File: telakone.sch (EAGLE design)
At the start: 166 parts, among them X10 MPT0.5/8-2.54, X11 MPT0.5/8-2.54, X2 MPT0.5/8-2.54, X3 MPT0.5/8-2.54, X4 PIIKKIRIMA-2, X5 PIIKKIRIMA-5, X7 U.FL-R-SMT-1, X8 MPT0.5/8-2.54, X9 629105136821

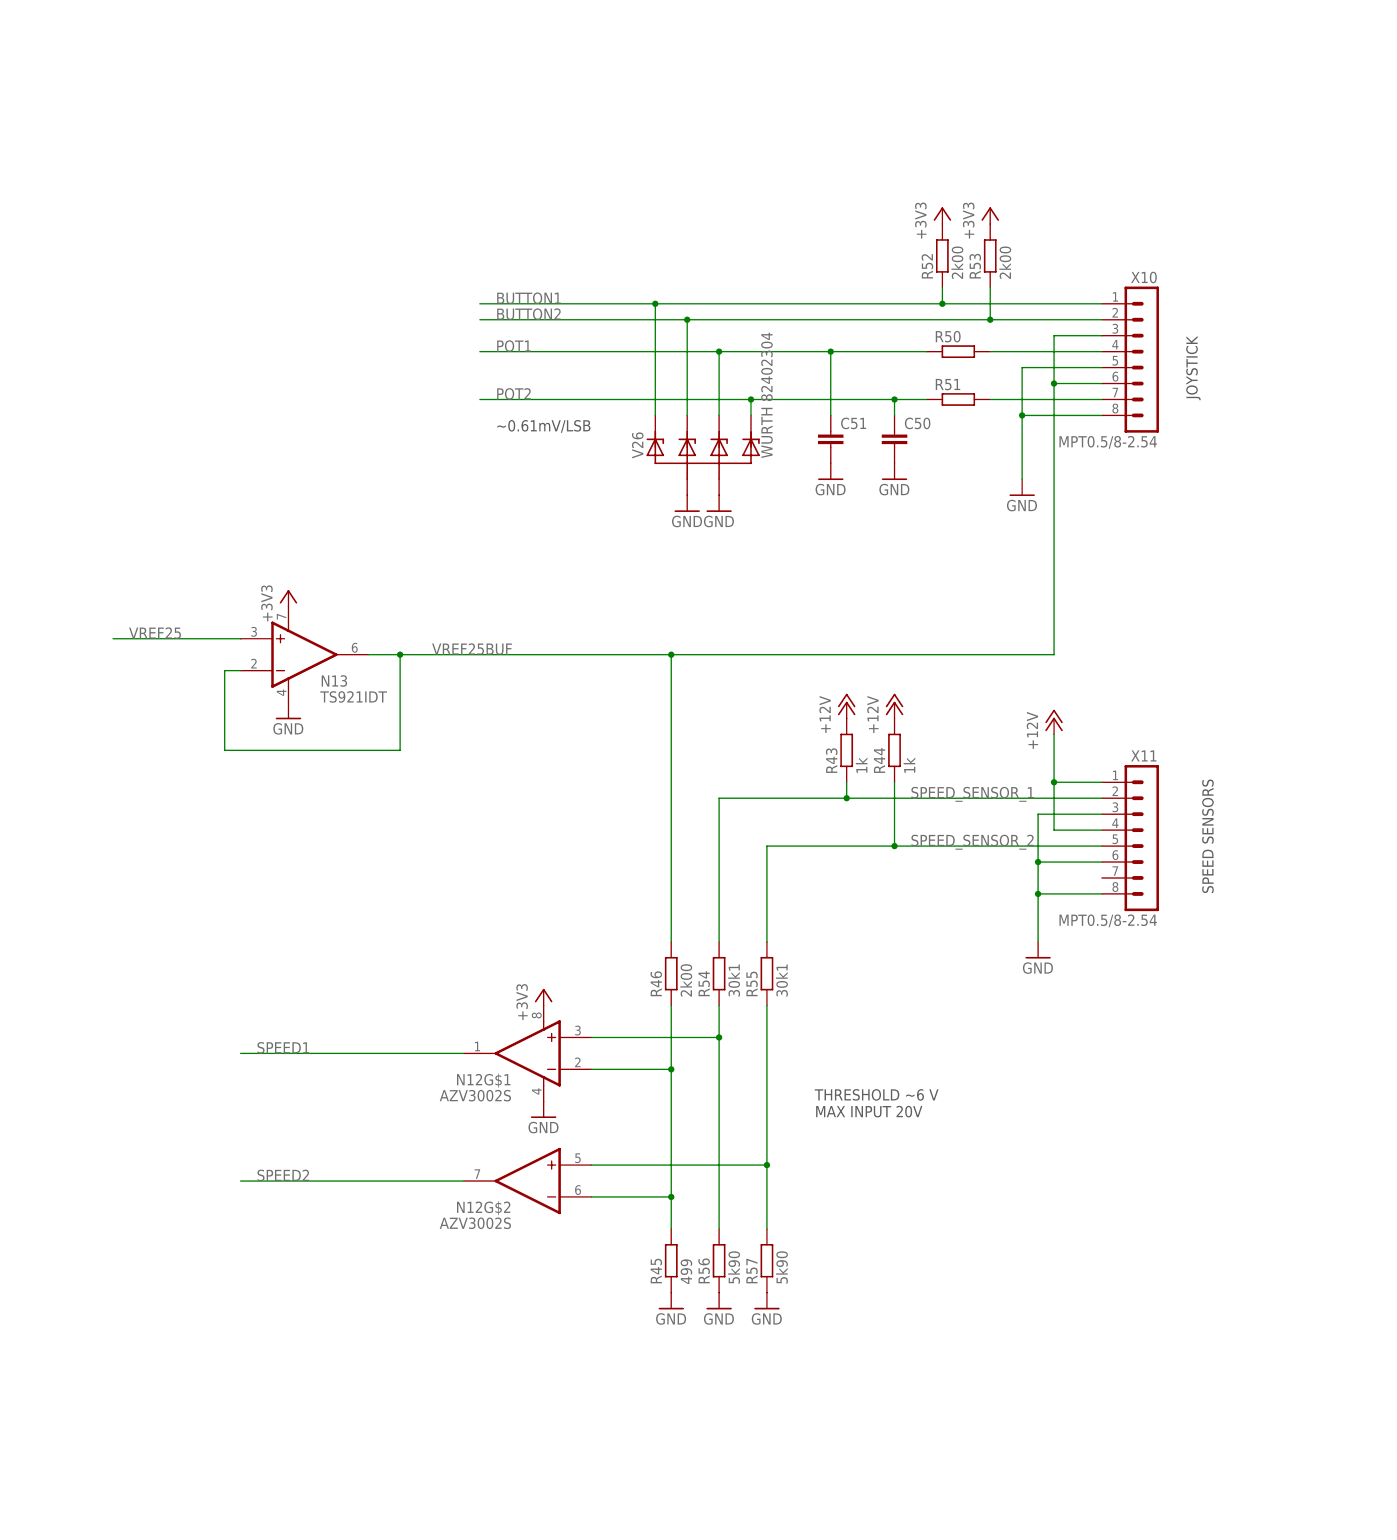
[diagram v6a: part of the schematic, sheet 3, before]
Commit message: add accessory link 485 transceiver
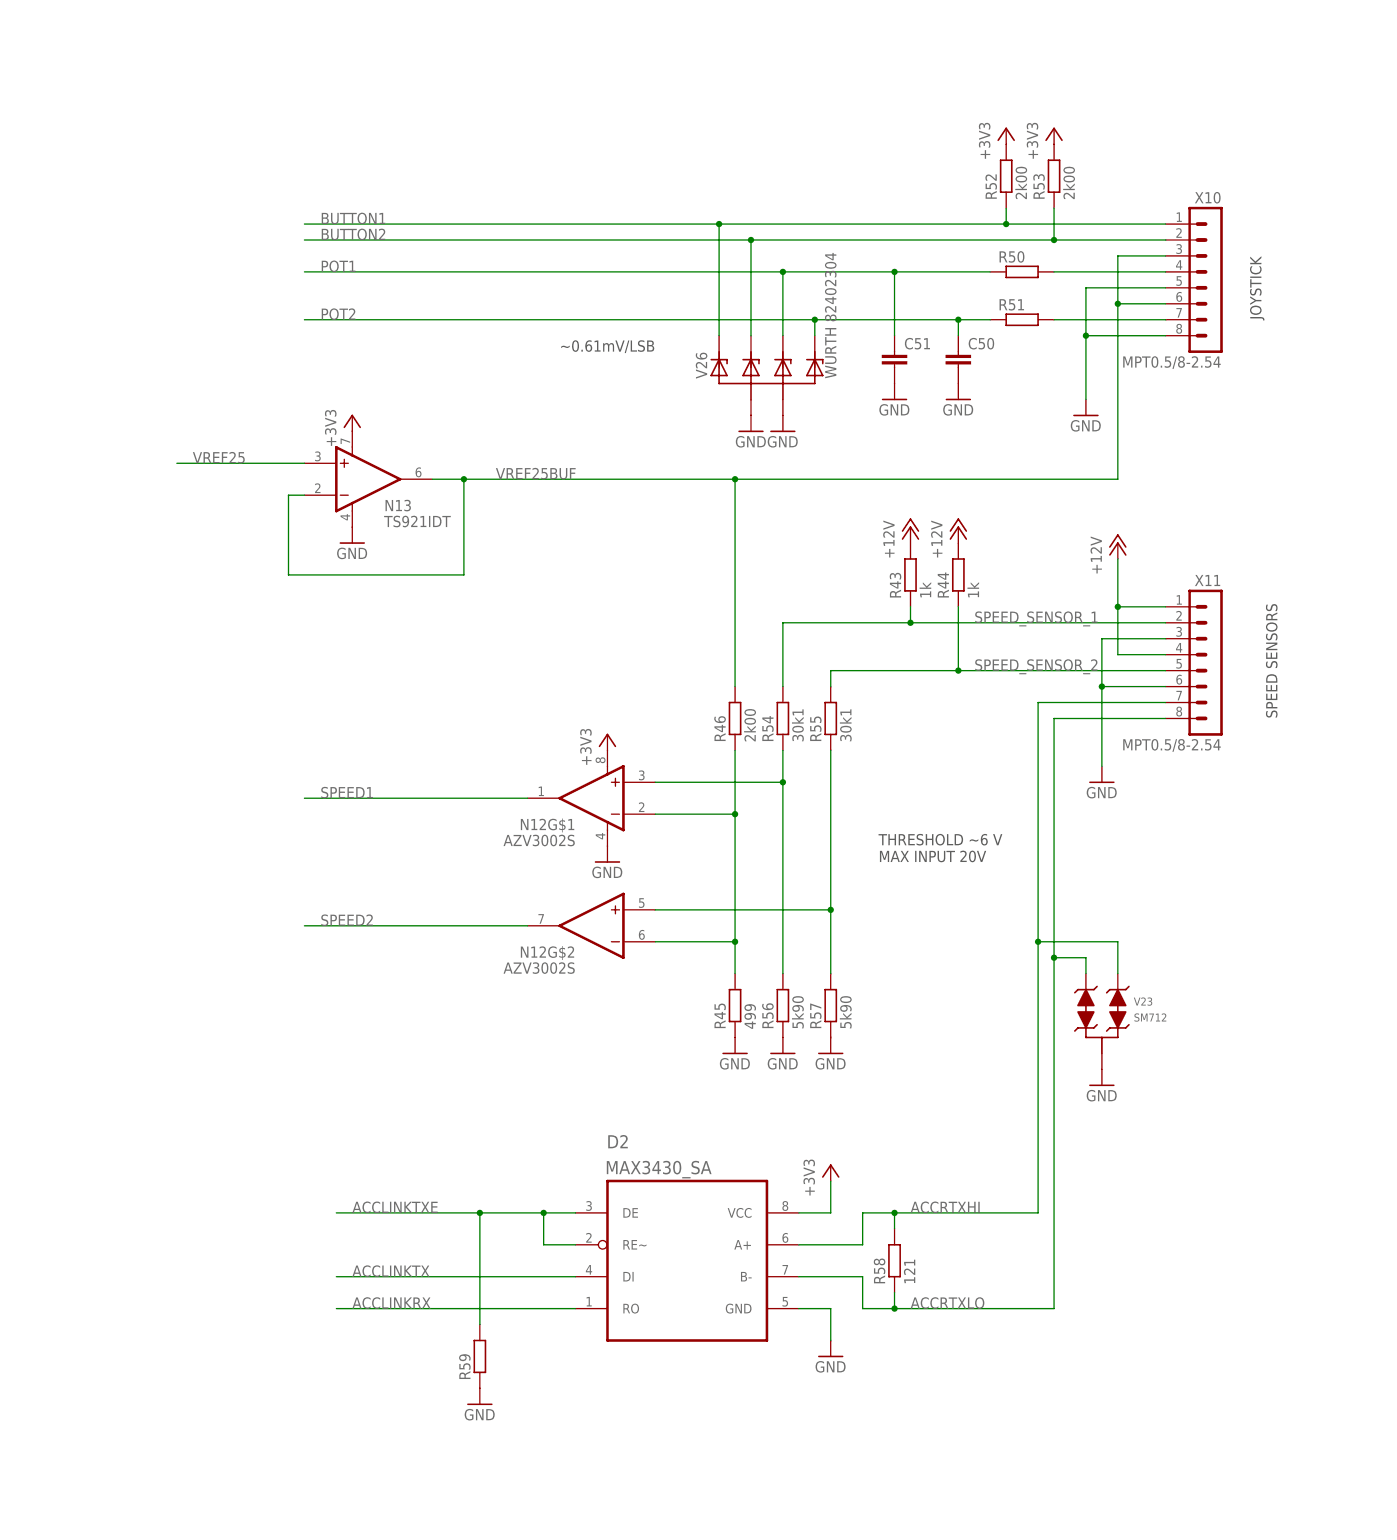
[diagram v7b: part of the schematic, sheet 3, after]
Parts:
- added D2: MAX3430_SA, omat_ic_2:MAX3088_SA
- added R58: 121, omat_ic_2:RES1206
- added R59: (no value), omat_ic_2:RES0603
- added V23: SM712, omat_ic_2:SM712
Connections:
- new net ACCLINKRX: D1G$2.PD6, D2.RO
- new net ACCLINKTX: D1G$2.PD5, D2.DI
- new net ACCLINKTXE: D1G$2.PD4, D2.DE, D2.RE~, R59.2
- new net ACCRTXHI: D2.A+, R58.2, V23.1, X11.7
- new net ACCRTXLO: D2.B-, R58.1, V23.2, X11.8
- net +3V3: now also D2.VCC
- net GND: now also D2.GND, R59.1, V23.3; no longer X11.8
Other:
- note added: "USART2"
- moved on the sheet: C50, C51, N12G$1, N12G$2, N13, R43, R44, R45, R46, R50, R51, R52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

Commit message: tuning
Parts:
- added V27: ESDAXXSC6, omat_ic_2:ESDAXXSC6
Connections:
- removed net N$25: R50.2, X10.4
- removed net N$43: R51.2, X10.7
- new net POT_IN_1: R50.2, V26.C2, X10.4
- new net POT_IN_2: R51.2, V26.C3, X10.7
- net GND: now also V27.A, V27.A1
- net POT1: no longer V26.C2
- net POT2: no longer V26.C3
- net SPEED_SENSOR_1: now also V27.C1
- net SPEED_SENSOR_2: now also V27.C2
- net VREF25BUF: now also V27.C
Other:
- moved on the sheet: C50, C51, R43, R44, R50, R51, V26, X10, X11
